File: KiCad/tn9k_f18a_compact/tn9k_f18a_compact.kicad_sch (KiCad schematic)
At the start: 27 parts, among them J2 VGA, J3 Tang Nano 9k, J4 TN9k/2, J6 VGA, U1 1G08, U4 74LCX16245

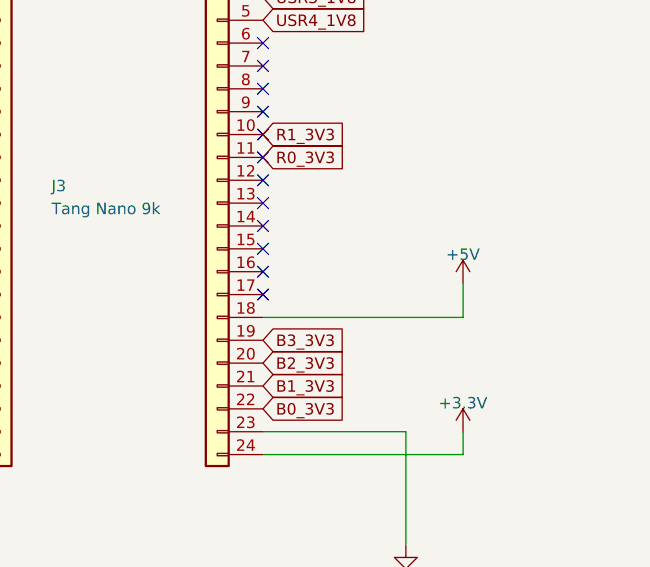
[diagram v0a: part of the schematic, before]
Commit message: Add diode to prevent host being powered from TN9k
HDMI has a +5V supply line that could halfway power up the TI-99/4A
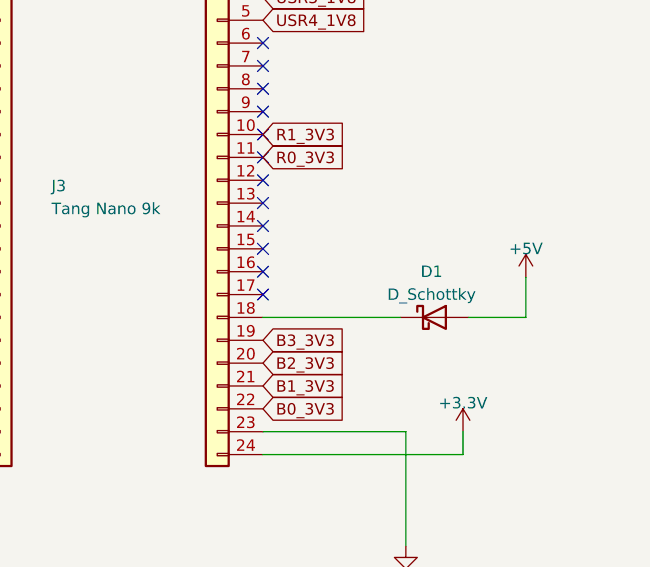
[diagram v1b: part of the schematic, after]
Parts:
- added D1: D_Schottky, Diode_SMD:D_SOD-123, symbol Device:D_Schottky
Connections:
- net +5V: now also D1.2 (A); no longer J4.18 (Pin_18)
- new net: D1.1 (K), J4.18 (Pin_18)

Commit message: Add BOM
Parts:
- C1: LCSC (none) -> C2857981
- D1: LCSC (none) -> C2900723
- R1, R5, R9: value 4.7K -> 4.42K; LCSC (none) -> C5140130
- R10, R2, R6: LCSC (none) -> C3016472
- R11, R3, R7: LCSC (none) -> C3016283
- R12, R4, R8: LCSC (none) -> C103660
- R13, R14: LCSC (none) -> C3016437
- U1: LCSC (none) -> C7666
- U4: LCSC (none) -> C894789
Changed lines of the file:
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@@
+      (effects (font (size 1.27 1.27)) hide)
+    )
+    (property "LCSC" "C3016437" (at 40.005 167.64 90)
       (effects (font (size 1.27 1.27)) hide)
     )
@@
       (effects (font (size 1.27 1.27)) hide)
     )
+    (property "LCSC" "C3016283" (at 55.245 128.27 90)
+      (effects (font (size 1.27 1.27)) hide)
+    )
     (pin "1")
     (pin "2")
@@
     )
     (property "Datasheet" "https://www.onsemi.com/pdf/datasheet/mc74lcx16245-d.pdf" (at 144.78 60.96 0)
+      (effects (font (size 1.27 1.27)) hide)
+    )
+    (property "LCSC" "C894789" (at 144.78 57.15 0)
       (effects (font (size 1.27 1.27)) hide)
     )
@@
       (effects (font (size 1.27 1.27)) hide)
     )
+    (property "LCSC" "C7666" (at 253.365 116.84 0)
+      (effects (font (size 1.27 1.27)) hide)
+    )
     (pin "1")
     (pin "2")
@@
       (effects (font (size 1.27 1.27)) hide)
     )
+    (property "LCSC" "C103660" (at 62.865 113.03 90)
+      (effects (font (size 1.27 1.27)) hide)
+    )
     (pin "1")
     (pin "2")
@@
       (effects (font (size 1.27 1.27)))
     )
-    (property "Value" "4.7K" (at 38.735 99.06 90)
+    (property "Value" "4.42K" (at 38.735 99.06 90)
       (effects (font (size 1.27 1.27)))
     )
@@
     )
     (property "Datasheet" "~" (at 38.735 101.6 0)
+      (effects (font (size 1.27 1.27)) hide)
+    )
+    (property "LCSC" "C5140130" (at 38.735 101.6 90)
       (effects (font (size 1.27 1.27)) hide)
     )
@@
     )
     (property "Datasheet" "~" (at 46.355 124.46 0)
+      (effects (font (size 1.27 1.27)) hide)
+    )
+    (property "LCSC" "C3016472" (at 46.355 124.46 90)
       (effects (font (size 1.27 1.27)) hide)
     )
@@
       (effects (font (size 1.27 1.27)) hide)
     )
+    (property "LCSC" "C3016283" (at 55.245 109.22 90)
+      (effects (font (size 1.27 1.27)) hide)
+    )
     (pin "1")
     (pin "2")
@@
     )
     (property "Datasheet" "~" (at 255.27 63.5 0)
+      (effects (font (size 1.27 1.27)) hide)
+    )
+    (property "LCSC" "C2900723" (at 255.27 63.5 0)
       (effects (font (size 1.27 1.27)) hide)
     )
@@
       (effects (font (size 1.27 1.27)))
     )
-    (property "Value" "4.7K" (at 38.735 137.16 90)
+    (property "Value" "4.42K" (at 38.735 137.16 90)
       (effects (font (size 1.27 1.27)))
     )
@@
       (effects (font (size 1.27 1.27)) hide)
     )
+    (property "LCSC" "C5140130" (at 38.735 139.7 90)
+      (effects (font (size 1.27 1.27)) hide)
+    )
     (pin "1")
     (pin "2")
@@
       (effects (font (size 1.27 1.27)) hide)
     )
+    (property "LCSC" "C103660" (at 62.865 132.08 90)
+      (effects (font (size 1.27 1.27)) hide)
+    )
     (pin "1")
     (pin "2")
@@
     )
     (property "Datasheet" "~" (at 62.865 151.13 0)
+      (effects (font (size 1.27 1.27)) hide)
+    )
+    (property "LCSC" "C103660" (at 62.865 151.13 90)
       (effects (font (size 1.27 1.27)) hide)
     )
@@
     )
     (property "Datasheet" "~" (at 55.245 147.32 0)
+      (effects (font (size 1.27 1.27)) hide)
+    )
+    (property "LCSC" "C3016283" (at 55.245 147.32 90)
       (effects (font (size 1.27 1.27)) hide)
     )
@@
       (effects (font (size 1.27 1.27)) hide)
     )
+    (property "LCSC" "C3016472" (at 46.355 143.51 90)
+      (effects (font (size 1.27 1.27)) hide)
+    )
     (pin "1")
     (pin "2")
@@
       (effects (font (size 1.27 1.27)) hide)
     )
+    (property "LCSC" "C2857981" (at 253.365 144.145 0)
+      (effects (font (size 1.27 1.27)) hide)
+    )
     (pin "1")
     (pin "2")
@@
       (effects (font (size 1.27 1.27)))
     )
-    (property "Value" "4.7K" (at 38.735 118.11 90)
+    (property "Value" "4.42K" (at 38.735 118.11 90)
       (effects (font (size 1.27 1.27)))
     )
@@
       (effects (font (size 1.27 1.27)) hide)
     )
+    (property "LCSC" "C5140130" (at 38.735 120.65 90)
+      (effects (font (size 1.27 1.27)) hide)
+    )
     (pin "1")
     (pin "2")
@@
       (effects (font (size 1.27 1.27)) hide)
     )
+    (property "LCSC" "C3016437" (at 40.005 160.02 90)
+      (effects (font (size 1.27 1.27)) hide)
+    )
     (pin "1")
     (pin "2")
@@
       (effects (font (size 1.27 1.27)) hide)
     )
+    (property "LCSC" "C3016472" (at 46.355 105.41 90)
+      (effects (font (size 1.27 1.27)) hide)
+    )
